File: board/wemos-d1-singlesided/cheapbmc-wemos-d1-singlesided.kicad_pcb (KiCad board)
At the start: 2 copper layers, 54 x 43.8 mm, 17 parts, among them J1 Conn_01x02_Male, J3 atxpanel, K1 SILxx-1Axx-71x, K2 SILxx-1Axx-71x, Q1 BC547, Q2 BC547, SW1 SW_Push, U2 FODM217A, U3 WeMos_D1_mini

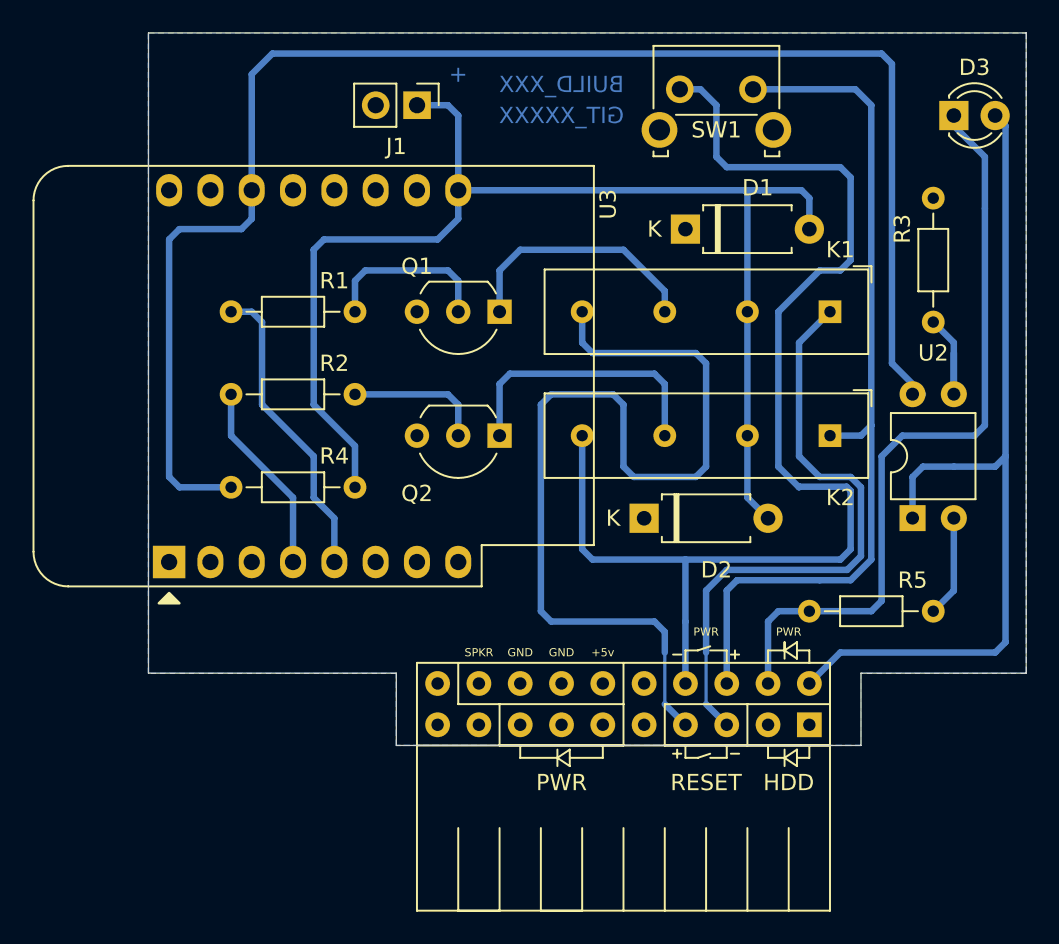
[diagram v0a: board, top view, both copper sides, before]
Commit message: wemos: avoid 0.8mm drill because of broken 0.8mm drill bit
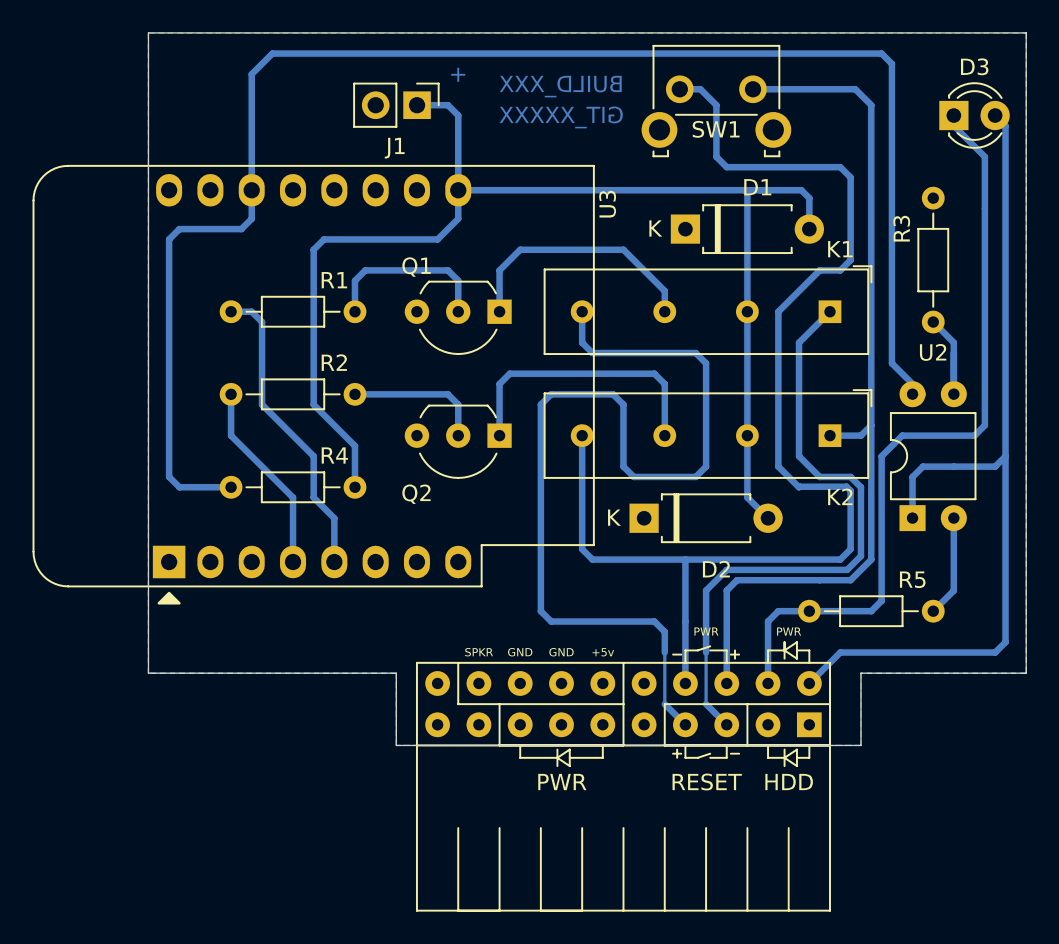
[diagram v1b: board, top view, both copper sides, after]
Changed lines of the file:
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@@
     (fp_arc (start 2.54 -2.48) (mid 4.831221 -0.949055) (end 4.293625 1.753625) (layer "F.Fab") (width 0.1))
     (fp_arc (start 0.786375 1.753625) (mid 0.248779 -0.949055) (end 2.54 -2.48) (layer "F.Fab") (width 0.1))
-    (pad "1" thru_hole rect locked (at 0 0 270) (size 1.5 1.5) (drill 0.8) (layers *.Cu *.Mask)
+    (pad "1" thru_hole rect locked (at 0 0 270) (size 1.5 1.5) (drill 0.7) (layers *.Cu *.Mask)
       (net 15 "Net-(K1-Pad5)") (pinfunction "C") (pintype "passive"))
-    (pad "2" thru_hole circle locked (at 2.54 0 270) (size 1.5 1.5) (drill 0.8) (layers *.Cu *.Mask)
+    (pad "2" thru_hole circle locked (at 2.54 0 270) (size 1.5 1.5) (drill 0.7) (layers *.Cu *.Mask)
       (net 11 "Net-(Q1-Pad2)") (pinfunction "B") (pintype "input"))
-    (pad "3" thru_hole circle locked (at 5.08 0 270) (size 1.5 1.5) (drill 0.8) (layers *.Cu *.Mask)
+    (pad "3" thru_hole circle locked (at 5.08 0 270) (size 1.5 1.5) (drill 0.7) (layers *.Cu *.Mask)
       (net 8 "GND") (pinfunction "E") (pintype "passive"))
     (model "${KISYS3DMOD}/Package_TO_SOT_THT.3dshapes/TO-92_Inline_Wide.wrl"
@@
     (fp_arc (start 2.54 -2.48) (mid 4.831221 -0.949055) (end 4.293625 1.753625) (layer "F.Fab") (width 0.1))
     (fp_arc (start 0.786375 1.753625) (mid 0.248779 -0.949055) (end 2.54 -2.48) (layer "F.Fab") (width 0.1))
-    (pad "1" thru_hole rect locked (at 0 0 270) (size 1.5 1.5) (drill 0.8) (layers *.Cu *.Mask)
+    (pad "1" thru_hole rect locked (at 0 0 270) (size 1.5 1.5) (drill 0.7) (layers *.Cu *.Mask)
       (net 16 "Net-(K2-Pad5)") (pinfunction "C") (pintype "passive"))
-    (pad "2" thru_hole circle locked (at 2.54 0 270) (size 1.5 1.5) (drill 0.8) (layers *.Cu *.Mask)
+    (pad "2" thru_hole circle locked (at 2.54 0 270) (size 1.5 1.5) (drill 0.7) (layers *.Cu *.Mask)
       (net 12 "Net-(Q2-Pad2)") (pinfunction "B") (pintype "input"))
-    (pad "3" thru_hole circle locked (at 5.08 0 270) (size 1.5 1.5) (drill 0.8) (layers *.Cu *.Mask)
+    (pad "3" thru_hole circle locked (at 5.08 0 270) (size 1.5 1.5) (drill 0.7) (layers *.Cu *.Mask)
       (net 8 "GND") (pinfunction "E") (pintype "passive"))
     (model "${KISYS3DMOD}/Package_TO_SOT_THT.3dshapes/TO-92_Inline_Wide.wrl"
@@
     (fp_line (start 1.635 -1.27) (end 6.985 -1.27) (layer "F.Fab") (width 0.1))
     (fp_line (start 0.635 -0.27) (end 1.635 -1.27) (layer "F.Fab") (width 0.1))
-    (pad "1" thru_hole rect locked (at 0 0 90) (size 1.6 1.6) (drill 0.8) (layers *.Cu *.Mask)
+    (pad "1" thru_hole rect locked (at 0 0 90) (size 1.6 1.6) (drill 0.7) (layers *.Cu *.Mask)
       (net 9 "PWRLED_P") (pintype "passive"))
-    (pad "2" thru_hole oval locked (at 0 2.54 90) (size 1.6 1.6) (drill 0.8) (layers *.Cu *.Mask)
+    (pad "2" thru_hole oval locked (at 0 2.54 90) (size 1.6 1.6) (drill 0.7) (layers *.Cu *.Mask)
       (net 17 "Net-(R5-Pad1)") (pintype "passive"))
-    (pad "3" thru_hole oval locked (at 7.62 2.54 90) (size 1.6 1.6) (drill 0.8) (layers *.Cu *.Mask)
+    (pad "3" thru_hole oval locked (at 7.62 2.54 90) (size 1.6 1.6) (drill 0.7) (layers *.Cu *.Mask)
       (net 13 "Net-(R3-Pad2)") (pintype "passive"))
-    (pad "4" thru_hole oval locked (at 7.62 0 90) (size 1.6 1.6) (drill 0.8) (layers *.Cu *.Mask)
+    (pad "4" thru_hole oval locked (at 7.62 0 90) (size 1.6 1.6) (drill 0.7) (layers *.Cu *.Mask)
       (net 14 "PWRLED_TTL") (pintype "passive"))
     (model "${KISYS3DMOD}/Package_DIP.3dshapes/DIP-4_W7.62mm.wrl"
@@
     (fp_line (start 10.668 2.794) (end 10.668 3.81) (layer "F.SilkS") (width 0.12))
     (fp_line (start 12.7 -2.54) (end 12.7 2.54) (layer "F.SilkS") (width 0.12))
-    (pad "1" thru_hole rect locked (at 11.43 1.27) (size 1.524 1.524) (drill 0.762) (layers *.Cu *.Mask)
+    (pad "1" thru_hole rect locked (at 11.43 1.27) (size 1.524 1.524) (drill 0.7) (layers *.Cu *.Mask)
       (net 18 "unconnected-(J3-Pad1)") (pinfunction "HDD_LED_P") (pintype "output"))
-    (pad "2" thru_hole circle locked (at 11.43 -1.27) (size 1.524 1.524) (drill 0.762) (layers *.Cu *.Mask)
+    (pad "2" thru_hole circle locked (at 11.43 -1.27) (size 1.524 1.524) (drill 0.7) (layers *.Cu *.Mask)
       (net 9 "PWRLED_P") (pinfunction "PWR_LED_P") (pintype "output"))
-    (pad "3" thru_hole circle locked (at 8.89 1.27) (size 1.524 1.524) (drill 0.762) (layers *.Cu *.Mask)
+    (pad "3" thru_hole circle locked (at 8.89 1.27) (size 1.524 1.524) (drill 0.7) (layers *.Cu *.Mask)
       (net 19 "unconnected-(J3-Pad3)") (pinfunction "HDD_LED_N") (pintype "output"))
-    (pad "4" thru_hole circle locked (at 8.89 -1.27) (size 1.524 1.524) (drill 0.762) (layers *.Cu *.Mask)
+    (pad "4" thru_hole circle locked (at 8.89 -1.27) (size 1.524 1.524) (drill 0.7) (layers *.Cu *.Mask)
       (net 10 "PWRLED_N") (pinfunction "PWR_LED_N") (pintype "output"))
-    (pad "5" thru_hole circle locked (at 6.35 1.27) (size 1.524 1.524) (drill 0.762) (layers *.Cu *.Mask)
+    (pad "5" thru_hole circle locked (at 6.35 1.27) (size 1.524 1.524) (drill 0.7) (layers *.Cu *.Mask)
       (net 2 "RSTCON_N") (pinfunction "RSTCON_N") (pintype "output"))
-    (pad "6" thru_hole circle locked (at 6.35 -1.27) (size 1.524 1.524) (drill 0.762) (layers *.Cu *.Mask)
+    (pad "6" thru_hole circle locked (at 6.35 -1.27) (size 1.524 1.524) (drill 0.7) (layers *.Cu *.Mask)
       (net 4 "PWRBTN_P") (pinfunction "PWRBTN_P") (pintype "output"))
-    (pad "7" thru_hole circle locked (at 3.81 1.27) (size 1.524 1.524) (drill 0.762) (layers *.Cu *.Mask)
+    (pad "7" thru_hole circle locked (at 3.81 1.27) (size 1.524 1.524) (drill 0.7) (layers *.Cu *.Mask)
       (net 1 "RSTCON_P") (pinfunction "RSTCON_P") (pintype "output"))
-    (pad "8" thru_hole circle locked (at 3.81 -1.27) (size 1.524 1.524) (drill 0.762) (layers *.Cu *.Mask)
+    (pad "8" thru_hole circle locked (at 3.81 -1.27) (size 1.524 1.524) (drill 0.7) (layers *.Cu *.Mask)
       (net 3 "PWRBTN_N") (pinfunction "PWRBTN_N") (pintype "output"))
-    (pad "9" thru_hole circle locked (at 1.27 1.27) (size 1.524 1.524) (drill 0.762) (layers *.Cu *.Mask))
-    (pad "10" thru_hole circle locked (at 1.27 -1.27) (size 1.524 1.524) (drill 0.762) (layers *.Cu *.Mask))
-    (pad "11" thru_hole circle locked (at -1.27 1.27) (size 1.524 1.524) (drill 0.762) (layers *.Cu *.Mask))
-    (pad "12" thru_hole circle locked (at -1.27 -1.27) (size 1.524 1.524) (drill 0.762) (layers *.Cu *.Mask))
-    (pad "13" thru_hole circle locked (at -3.81 1.27) (size 1.524 1.524) (drill 0.762) (layers *.Cu *.Mask))
-    (pad "14" thru_hole circle locked (at -3.81 -1.27) (size 1.524 1.524) (drill 0.762) (layers *.Cu *.Mask))
-    (pad "15" thru_hole circle locked (at -6.35 1.27) (size 1.524 1.524) (drill 0.762) (layers *.Cu *.Mask))
-    (pad "16" thru_hole circle locked (at -6.35 -1.27) (size 1.524 1.524) (drill 0.762) (layers *.Cu *.Mask))
-    (pad "17" thru_hole circle locked (at -8.89 1.27) (size 1.524 1.524) (drill 0.762) (layers *.Cu *.Mask))
-    (pad "18" thru_hole circle locked (at -8.89 -1.27) (size 1.524 1.524) (drill 0.762) (layers *.Cu *.Mask))
-    (pad "19" thru_hole circle locked (at -11.43 -1.27) (size 1.524 1.524) (drill 0.762) (layers *.Cu *.Mask))
-    (pad "20" thru_hole circle locked (at -11.43 1.27) (size 1.524 1.524) (drill 0.762) (layers *.Cu *.Mask))
+    (pad "9" thru_hole circle locked (at 1.27 1.27) (size 1.524 1.524) (drill 0.7) (layers *.Cu *.Mask))
+    (pad "10" thru_hole circle locked (at 1.27 -1.27) (size 1.524 1.524) (drill 0.7) (layers *.Cu *.Mask))
+    (pad "11" thru_hole circle locked (at -1.27 1.27) (size 1.524 1.524) (drill 0.7) (layers *.Cu *.Mask))
+    (pad "12" thru_hole circle locked (at -1.27 -1.27) (size 1.524 1.524) (drill 0.7) (layers *.Cu *.Mask))
+    (pad "13" thru_hole circle locked (at -3.81 1.27) (size 1.524 1.524) (drill 0.7) (layers *.Cu *.Mask))
+    (pad "14" thru_hole circle locked (at -3.81 -1.27) (size 1.524 1.524) (drill 0.7) (layers *.Cu *.Mask))
+    (pad "15" thru_hole circle locked (at -6.35 1.27) (size 1.524 1.524) (drill 0.7) (layers *.Cu *.Mask))
+    (pad "16" thru_hole circle locked (at -6.35 -1.27) (size 1.524 1.524) (drill 0.7) (layers *.Cu *.Mask))
+    (pad "17" thru_hole circle locked (at -8.89 1.27) (size 1.524 1.524) (drill 0.7) (layers *.Cu *.Mask))
+    (pad "18" thru_hole circle locked (at -8.89 -1.27) (size 1.524 1.524) (drill 0.7) (layers *.Cu *.Mask))
+    (pad "19" thru_hole circle locked (at -11.43 -1.27) (size 1.524 1.524) (drill 0.7) (layers *.Cu *.Mask))
+    (pad "20" thru_hole circle locked (at -11.43 1.27) (size 1.524 1.524) (drill 0.7) (layers *.Cu *.Mask))
   )
   (footprint "Module:WEMOS_D1_mini_light" (layer "F.Cu")
